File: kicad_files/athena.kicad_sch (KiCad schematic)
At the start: 540 parts, among them J1 SM04B-SRSS-TB(LF)(SN), J2 TYPE-C-31-M12, J3 SM04B-SRSS-TB(LF)(SN), Q1 DTC123JKAT146, Q2 AO3401A, SW1 K2-1187SQ-A4SW-06, SW10 MX Switch, SW100 MX Switch, SW101 MX Switch, SW102 MX Switch, SW103 MX Switch, SW104 MX Switch, SW105 MX Switch, SW106 MX Switch, SW107 MX Switch, SW108 MX Switch, SW109 MX Switch, SW11 MX Switch, SW110 MX Switch, SW111 MX Switch, SW112 MX Switch, SW113 MX Switch, SW12 MX Switch, SW13 MX Switch, SW14 MX Switch, SW15 MX Switch, SW16 MX Switch, SW17 MX Switch, SW18 MX Switch, SW19 MX Switch, SW2 MX Switch, SW20 MX Switch, SW21 MX Switch, SW22 MX Switch, SW23 MX Switch, SW24 MX Switch, SW25 MX Switch, SW26 MX Switch, SW27 MX Switch, SW28 MX Switch, SW29 MX Switch, SW3 MX Switch, SW30 MX Switch, SW31 MX Switch, SW32 MX Switch, SW33 MX Switch, SW34 MX Switch, SW35 MX Switch, SW36 MX Switch, SW37 MX Switch, SW38 MX Switch, SW39 MX Switch, SW4 MX Switch, SW40 MX Switch, SW41 MX Switch, SW42 MX Switch, SW43 MX Switch, SW44 MX Switch, SW45 MX Switch, SW46 MX Switch, SW47 MX Switch, SW48 MX Switch, SW49 MX Switch, SW5 MX Switch, SW50 MX Switch, SW51 MX Switch, SW52 MX Switch, SW53 MX Switch, SW54 MX Switch, SW55 MX Switch, SW56 MX Switch, SW57 MX Switch, SW58 MX Switch, SW59 MX Switch, SW6 MX Switch, SW60 MX Switch, SW61 MX Switch, SW62 MX Switch, SW63 MX Switch, SW64 MX Switch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

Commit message: Update component metadata
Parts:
- C16, C17, C5: Package C3216 -> C3216 (CASE A)
- D10, D11, D12, D13, D14, D15, D16, D17, D18, D19, D20, D21, D22, D23, D24, D25, D26, D27, D28, D29, D30, D31, D32, D33, D34, D35, D36, D4, D5, D6, D7, D8, D9: Manufacturer Part Number LCSC C965556 (https://www.lcsc.com/product-detail/Light-Emi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 -> WS2812C-2020; Vendor Part Number WS2812C-2020 -> LCSC C965556
- D2: LCSC Part Number C114257 -> (none); Vendor Part Number (none) -> LCSC C114257
- F1: LCSC Part Number C69691 -> (none); Vendor Part Number (none) -> LCSC C69691
- FB1, FB2: LCSC Part Number C139186 -> (none); Vendor Part Number (none) -> LCSC C139186
- J1, J3: LCSC Part Number C160404 -> (none); Vendor Part Number (none) -> LCSC C160404
- J2: LCSC Part Number C165948 -> (none); Specification (none) -> 16-pin USB 2.0 type C connector; Vendor Part Number (none) -> LCSC C165948
- Q1: LCSC Part Number C111724 -> (none); Vendor Part Number (none) -> LCSC C111724
- SW1: LCSC Part Number C92584 -> (none); Vendor Part Number (none) -> LCSC C92584
- SW10, SW100, SW101, SW102, SW103, SW104, SW105, SW106, SW107, SW108, SW109, SW11, SW110, SW111, SW112, SW113, SW12, SW13, SW14, SW15, SW16, SW17, SW18, SW19, SW2, SW20, SW21, SW22, SW23, SW24, SW25, SW26, SW27, SW28, SW29, SW3, SW30, SW31, SW32, SW33, SW34, SW35, SW36, SW37, SW38, SW39, SW4, SW40, SW41, SW42, SW43, SW44, SW45, SW46, SW47, SW48, SW49, SW5, SW50, SW51, SW52, SW53, SW54, SW55, SW56, SW57, SW58, SW59, SW6, SW60, SW61, SW62, SW63, SW64, SW65, SW66, SW67, SW68, SW69, SW7, SW70, SW71, SW72, SW73, SW74, SW75, SW76, SW77, SW78, SW79, SW8, SW80, SW81, SW82, SW83, SW84, SW85, SW86, SW87, SW88, SW89, SW9, SW90, SW91, SW92, SW93, SW94, SW95, SW96, SW97, SW98, SW99: Manufacturer Kaihua -> (none); Specification MX-style switch socket -> MX-style mechanical keyboard switch
- U3: LCSC Part Number C132604 -> (none); Vendor Part Number (none) -> LCSC C132604
- U4: LCSC Part Number C7519 -> (none); Vendor Part Number (none) -> LCSC C7519
- U5: LCSC Part Number C39051 -> (none); Vendor Part Number (none) -> LCSC C39051

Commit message: Re-routes, optimizations, corrections
- Re-routed rows R4 and R5; SWCLK pin confirmedly works as row pin as tested on pre-revision Alpha prototypes
- Removec trace stubs on bottom left
- Small traces optimization
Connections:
- net SWCLK is gone; now on net R5: U2.37 (PA14), X1.2 (Pin_2)
- net R4: now also U2.3 (PC14_OSC32IN)
- net R5: no longer U2.3 (PC14_OSC32IN)

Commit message: a-RC1 label, digital transistors
- Label was changed to Alpha-RC1 version
- Instead of relying on MCU open-drain pins, discrete digital NPN transistors were added to the caps lock indicator control and backlight PWM opendrain circuit
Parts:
- added Q3, Q4: DTC123JKAT146, Package_TO_SOT_SMD:SOT-23, symbol acheronSymbols:DTC123J
- GR6: renamed from GR4; footprint athena_library:athena_letters_pre-alpha_35x5.6 -> athena_library:athena_label_35x5.6
- renumbered C13 to C1, C6 to C10, C7 to C11, C16 to C12, C17 to C13, C19 to C14, C8 to C15, C9 to C16, C10 to C17, C11 to C18, C20 to C19, C14 to C2, C21 to C20, C22 to C21, C23 to C22, C24 to C23, C25 to C24, C26 to C25, C27 to C26, C28 to C27, C29 to C28, C30 to C29, C1 to C3, C31 to C30, C32 to C31, C33 to C32, C34 to C33, C35 to C34, C36 to C35, C37 to C36, C38 to C37, C39 to C38, C40 to C39, C2 to C4, C41 to C40, C42 to C41, C43 to C42, C44 to C43, C45 to C44, C46 to C45, C47 to C46, C48 to C47, C49 to C48, C50 to C49, C3 to C5, C51 to C50, C52 to C51, C15 to C6, C4 to C7, C18 to C8, C5 to C9, GR7 to GR2, GR2 to GR3, GR8 to GR4, GR3 to GR5, GR5 to GR7, GR6 to GR8, LED99 to LED100, LED100 to LED101, LED101 to LED102, LED102 to LED103, LED103 to LED104, LED104 to LED105, LED105 to LED106, LED106 to LED107, LED107 to LED108, LED108 to LED109, LED109 to LED110, LED69 to LED68, LED68 to LED69, LED94 to LED91, LED91 to LED92, LED92 to LED93, LED93 to LED94, LED110 to LED95, LED95 to LED96, LED96 to LED97, LED97 to LED98, LED98 to LED99, R11 to R10, R109 to R108, R110 to R109, R7 to R11, R108 to R110, R5 to R3, R3 to R4, R10 to R5, R4 to R6, R8 to R7, R9 to R8, R87 to R86, R88 to R87, R89 to R88, R90 to R89, R6 to R9, R91 to R90, R92 to R91, R93 to R92, R94 to R93, R95 to R94, R96 to R95, R97 to R96, R98 to R97, R86 to R98, U3 to U1, U4 to U2, U1 to U3, U2 to U4, X2 to X1, X1 to X2
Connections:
- net CAPS_INDICATOR: now also Q4.1 (B); no longer LED68.K, LED69.K
- net GND: now also Q3.2 (E), Q4.2 (E)
- net LED_PWM: now also Q3.1 (B); no longer R14.1, R15.1
- new net: Q3.3 (C), R14.1, R15.1
- new net: LED68.K, LED69.K, Q4.3 (C)

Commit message: Start porting to 64 pin MCU
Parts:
- removed C4, C5, C7: 100n, Capacitor_SMD:C_0402_1005Metric, symbol Device:C_Small
- removed R1, R2, R4: 1.5k, Resistor_SMD:R_0402_1005Metric, symbol Device:R_Small
- removed U4: STM32F411CEU6, acheron_Components:STM_UFQFPN-48_LQFP-48-1EP_7x7mm_P0.5mm_HandSoldering_ThermalReliefs, symbol acheron_Symbols:STM32F411-48
- added C15, C19: 4.7u, Capacitor_SMD:C_0402_1005Metric, symbol Device:C_Small
- added C16: 10n, Capacitor_SMD:C_0402_1005Metric, symbol Device:C_Small
- added C8: 100n, Capacitor_SMD:C_0402_1005Metric, symbol Device:C_Small
- added R7: 4.7k, Resistor_SMD:R_0402_1005Metric, symbol Device:R_Small
- added U5: STM32F401RCT6, acheron_Components:LQFP-64_10x10mm_P0.5mm, symbol acheronSymbols:STM32F401-LQFP64
- C10: value 1u -> 100n
- C11: value 10n -> 100n
- C18: value 4.7u -> 100n
- R6: value 0R -> 4.7k; footprint Resistor_SMD:R_0805_2012Metric -> Resistor_SMD:R_0402_1005Metric; Package R0805 -> R0402
- U3: value BL24C256A-SFRC -> 24LC256-I/SN; footprint acheron_Components:TSSOP-8_4.4x3mm_P0.65mm -> acheron_Components:SOIC-8; Manufacturer Shanghai Belling -> Microchip; Manufacturer Part Number BL24C256A-SFRC -> 24LC256-I/SN; Package TSSOP-8 -> SOIC-8; Specification TSSOP-8 non-volatile 256Kb (32K x 8) I2C EEPROM -> SOIC-8 non-volatile 256Kb (32K x 8) I2C EEPROM; Vendor Part Number LCSC C691875 (https://lcsc.com/product-detail/EEPROM_BL-Sha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 -> LCSC C411625
- renumbered C9 to C12, C15 to C13, C16 to C14, C19 to C20, C20 to C21, C21 to C22, C22 to C23, C23 to C24, C24 to C25, C25 to C26, C26 to C27, C27 to C28, C28 to C29, C29 to C30, C30 to C31, C31 to C32, C32 to C33, C33 to C34, C34 to C35, C35 to C36, C36 to C37, C37 to C38, C38 to C39, C6 to C4, C39 to C40, C40 to C41, C41 to C42, C42 to C43, C43 to C44, C44 to C45, C45 to C46, C46 to C47, C47 to C48, C48 to C49, C8 to C5, C49 to C50, C50 to C51, C51 to C52, C12 to C6, C13 to C7, C14 to C9, R3 to R1, R12 to R10, R102 to R100, R103 to R101, R104 to R102, R105 to R103, R106 to R104, R107 to R105, R108 to R106, R109 to R107, R110 to R108, R13 to R11, R14 to R12, R15 to R13, R16 to R14, R17 to R15, R18 to R16, R19 to R17, R20 to R18, R21 to R19, R5 to R2, R22 to R20, R23 to R21, R24 to R22, R25 to R23, R26 to R24, R27 to R25, R28 to R26, R29 to R27, R30 to R28, R31 to R29, R7 to R3, R32 to R30, R33 to R31, R34 to R32, R35 to R33, R36 to R34, R37 to R35, R38 to R36, R39 to R37, R40 to R38, R41 to R39, R8 to R4, R42 to R40, R43 to R41, R44 to R42, R45 to R43, R46 to R44, R47 to R45, R48 to R46, R49 to R47, R50 to R48, R51 to R49, R9 to R5, R52 to R50, R53 to R51, R54 to R52, R55 to R53, R56 to R54, R57 to R55, R58 to R56, R59 to R57, R60 to R58, R61 to R59, R62 to R60, R63 to R61, R64 to R62, R65 to R63, R66 to R64, R67 to R65, R68 to R66, R69 to R67, R70 to R68, R71 to R69, R72 to R70, R73 to R71, R74 to R72, R75 to R73, R76 to R74, R77 to R75, R78 to R76, R79 to R77, R80 to R78, R81 to R79, R10 to R8, R82 to R80, R83 to R81, R84 to R82, R85 to R83, R86 to R84, R87 to R85, R88 to R86, R89 to R87, R90 to R88, R91 to R89, R11 to R9, R92 to R90, R93 to R91, R94 to R92, R95 to R93, R96 to R94, R97 to R95, R98 to R96, R99 to R97, R100 to R98, R101 to R99, U5 to U4
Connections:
- net 3V3: now also C18.1, R6.2, C15.2, C16.2, C8.2, R7.2, U5.1 (VBAT), U5.13 (VDDA/VREF+), U5.19 (VDD), U5.32 (VDD), U5.48 (VDD), U5.64 (VDD)
- net 5V: no longer R6.1
- net BOOT0: now also C9.1, R10.1, R8.1, U5.60 (BOOT0); no longer C9.2, R10.2, R8.2
- net C0: now also U5.38 (USART6_RX/TIM3_CH2/PC7)
- net C1: now also U5.37 (I2S2_MCK/TIM3_CH1/USART6_TX/PC6)
- net C10: now also U5.20 (PA4/USART2_CK)
- net C11: now also U5.17 (PA3/TIM2_CH4/USART2_RX)
- net C12: now also U5.16 (PA2/TIM2_CH3/USART2_TX)
- net C13: now also U5.25 (PC5)
- net C14: now also U5.43 (USART1_RX/TIM1_CH3/PA10)
- net C15: now also U5.41 (USART1_CK/TIM1_CH1/PA8)
- net C16: now also U5.40 (TIM3_CH4/I2S_CKIN/PC9)
- net C2: now also U5.35 (SPI2_MISO/PB14)
- net C3: now also U5.33 (PB12)
- net C4: now also U5.29 (PB10/TIM2_CH3/SPI2_SCK/I2C2_SCL/I2S2_CK)
- net C5: now also U5.27 (PB1/TIM3_CH4)
- net C6: now also U5.24 (PC4)
- net C7: now also U5.23 (PA7/SPI1_MOSI/TIM3_CH2)
- net C8: now also U5.22 (PA6/TIM3_CH1/SPI1_MISO)
- net C9: now also U5.21 (PA5/TIM2_CH1/SPI1_SCK)
- net CAPS_INDICATOR: now also U5.39 (USART6_CK/TIM3_CH3/PC8)
- net D+: now also U5.45 (OTG_FS_DP/USART6_RX/PA12)
- net D-: now also U5.44 (OTG_FS_DM/TIM1_CH4/USART6_TX/PA11)
- net GND: now also C18.2, C9.2, R10.2, C15.1, C16.1, C19.1, C8.1, U5.12 (VSSA/VREF-), U5.18 (VSS), U5.31 (VSS), U5.47 (VSS), U5.63 (VSS); no longer C18.1, C9.1, R10.1
- net LED_PWM: now also U5.26 (PB0/TIM3_CH3)
- net NRST: now also U5.7 (NRST)
- net PA9: now also U5.42 (USART1_TX/TIM1_CH2/PA9); no longer R6.2
- net PB2/BOOT1: now also U5.28 (PB2)
- net R0: now also U5.52 (SPI3_MISO/PC11)
- net R1: now also U5.53 (SPI3_MOSI/PC12)
- net R2: now also U5.51 (SPI3_SCK/I2S3_CK/PC10)
- net R3: now also U5.50 (JTDI/TIM2_CH1/PA14)
- net R5: no longer X2.2 (Pin_2)
- net RGB_3V3: now also U5.36 (SPI2_MOSI/PB15)
- net SCL: now also R7.1, U5.58 (I2C1_SCL/USART1_TX/TIM4_CH1/PB6)
- net SDA: now also R6.1, U5.59 (I2C1_SDA/USART1_RX/TIM4_CH2/PB7)
- net SWDIO: now also U5.46 (JTMS-SWDIO/PA13)
- net XTAL_IN: now also U5.5 (PH0/OSC_IN)
- net XTAL_OUT: now also U5.6 (PH1/OSC_OUT)
- net at D3.1 (K): now also R8.2; no longer R8.1
- new net: C19.2, U5.30 (VCAP1)
- new net SWCLK: U5.49 (JTCK-SWCLK/PA14), X2.2 (Pin_2)
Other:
- note added: "SPOOKY PIN"
- note removed: "Spooky pin (*)"
- moved on the sheet: C12, C13, C14, C9, R10, R8, X2, Y1

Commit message: hange LDO caps to MLCC
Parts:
- removed C6, C7: 1u, acheron_Components:CP_EIA-3216-10_Kemet-I_Pad1.58x1.35mm_HandSolder, symbol Device:CP1
- added C6, C7: 1u, Capacitor_SMD:C_0805_2012Metric, symbol Device:C
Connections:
- net 3V3: now also C7.1
- net 5V: now also C6.1
- net GND: now also C6.2, C7.2
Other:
- moved on the sheet: C13, C14, Y1

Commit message: Update libs, route extra pins
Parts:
- added R12: 0R, Resistor_SMD:R_0805_2012Metric, symbol Device:R_Small
- renumbered R99 to R100, R100 to R101, R101 to R102, R102 to R103, R103 to R104, R104 to R105, R105 to R106, R106 to R107, R107 to R108, R108 to R109, R12 to R13, R13 to R14, R14 to R15, R15 to R16, R16 to R17, R17 to R18, R18 to R19, R19 to R20, R20 to R21, R21 to R22, R22 to R23, R23 to R24, R24 to R25, R25 to R26, R26 to R27, R27 to R28, R28 to R29, R29 to R30, R30 to R31, R31 to R32, R32 to R33, R33 to R34, R34 to R35, R35 to R36, R36 to R37, R37 to R38, R38 to R39, R39 to R40, R40 to R41, R41 to R42, R42 to R43, R43 to R44, R44 to R45, R45 to R46, R46 to R47, R47 to R48, R48 to R49, R49 to R50, R50 to R51, R51 to R52, R52 to R53, R53 to R54, R54 to R55, R55 to R56, R56 to R57, R57 to R58, R58 to R59, R59 to R60, R60 to R61, R61 to R62, R62 to R63, R63 to R64, R64 to R65, R65 to R66, R66 to R67, R67 to R68, R68 to R69, R69 to R70, R70 to R71, R71 to R72, R72 to R73, R73 to R74, R74 to R75, R75 to R76, R76 to R77, R77 to R78, R78 to R79, R79 to R80, R80 to R81, R81 to R82, R82 to R83, R83 to R84, R84 to R85, R85 to R86, R86 to R87, R87 to R88, R88 to R89, R89 to R90, R90 to R91, R91 to R92, R92 to R93, R93 to R94, R94 to R95, R95 to R96, R96 to R97, R97 to R98, R98 to R99
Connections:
- net 5V: now also R12.2
- net PA9: now also R12.1
- net R4: now also U5.14 (PA0/TIM2_CH1/USART2_CTS)
- net R5: now also U5.15 (PA1/TIM2_CH2/USART2_RTS)
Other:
- moved on the sheet: C1, C10, C11, C12, C13, C14, C15, C16, C17, C18, C19, C2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

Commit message: Add some extra pins
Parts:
- added J3: Conn_02x07_Counter_Clockwise, acheron_Connectors:PinHeader_2x3_P2.54mm_Vertical, symbol Connector_Generic:Conn_02x03_Odd_Even
- renumbered C8 to C1, C14 to C10, C9 to C11, C15 to C12, C16 to C13, C17 to C14, C18 to C15, C19 to C16, C1 to C17, C2 to C18, C4 to C19, C3 to C2, C10 to C3, C11 to C4, C12 to C6, C6 to C7, C7 to C8, C13 to C9, D2 to D1, D3 to D2, D1 to D3, J2 to J1, J3 to J2, J1 to J4, R6 to R1, R1 to R12, R7 to R2, R12 to R3, R2 to R4, R3 to R5, R4 to R6, R5 to R7, U2 to U1, U3 to U2, U5 to U3, U1 to U5
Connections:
- net 3V3: now also J3.4 (Pin_4)
- net C14: now also SW104.2; no longer SW104.1
- net GND: now also J3.2 (Pin_2)
- net R4: now also U3.8 (PC0); no longer U3.14 (PA0/TIM2_CH1/USART2_CTS)
- net at D126.2 (A): now also SW104.1; no longer SW104.2
- net E-PC2: now reaches U3.10 (PC2/SPI2_MISO)
- net E-PC2: now also J3.5 (Pin_5)
- net E-PC3: now reaches U3.11 (PC3/SPI2_MOSI)
- net E-PC3: now also J3.3 (Pin_3)
- net E-PC13: now reaches U3.2 (PC13)
- net E-PC14: now reaches U3.3 (PC14/OSC32_IN)
- net E-PC15: now reaches U3.4 (PC15/OSC32_OUT)
- net E-PD2: now reaches U3.54 (PD2)
- net E-PB3: now reaches U3.55 (JTDO-SWO/SPI1_SCK/SPI3_SCK/I2C2_SDA/TIM2_CH2/PB3)
- net E-PB4: now reaches U3.56 (NJTRST/SPI1_MISO/SPI3_MISO/I2C3_SDA/TIM3_CH1/PB4)
- net E-PB5: now reaches U3.57 (SPI1_MOSI/SPI3_MOSI/TIM3_CH2/PB5)
- net E-PB8: now reaches U3.61 (I2C1_SCL/TIM4_CH3/TIM10_CH1/PB8)
- net E-PB9: now reaches U3.62 (I2C1_SDA/TIM4_CH4/TIM11_CH1/PB9)
- net E-PC1: now reaches U3.9 (PC1)
- net E-PC1: now also J3.6 (Pin_6)
- new net E-PA0: J3.1 (Pin_1), U3.14 (PA0/TIM2_CH1/USART2_CTS)
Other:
- moved on the sheet: SW104

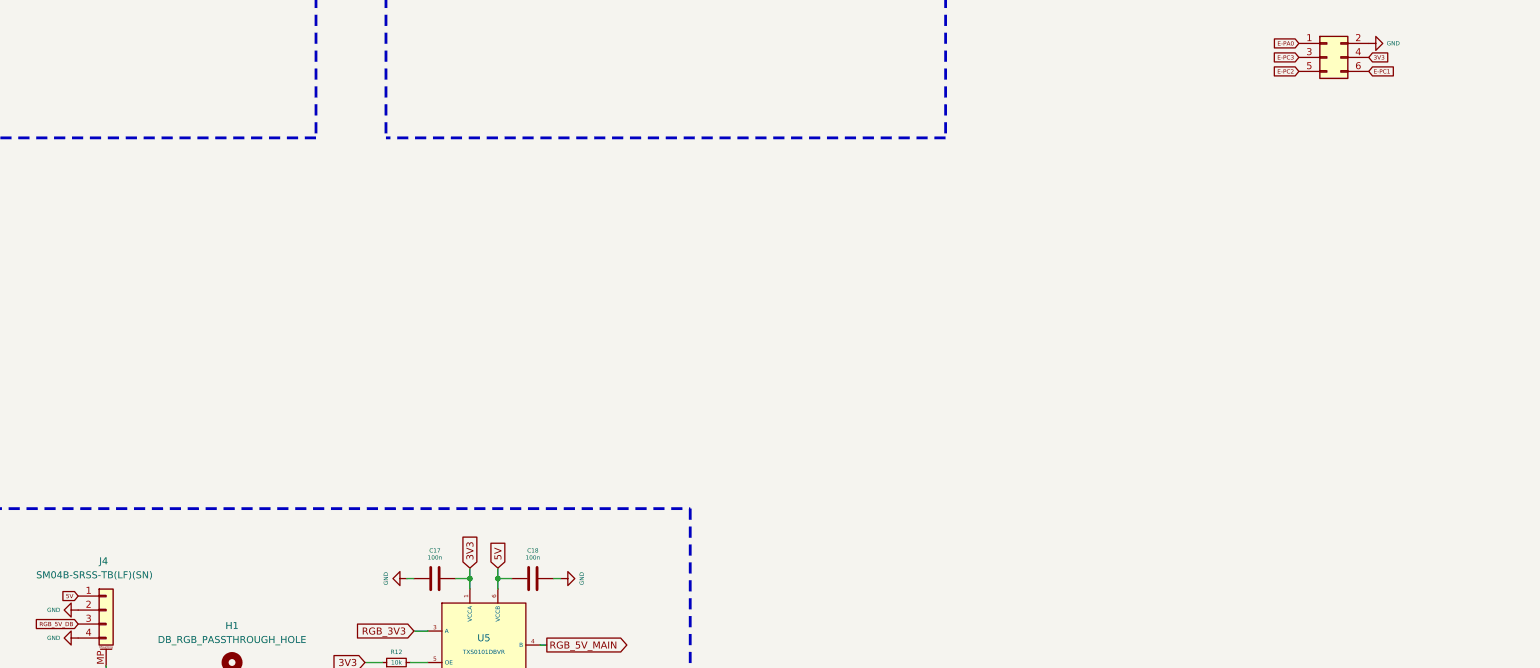
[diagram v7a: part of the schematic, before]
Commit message: Finish adding extra pins
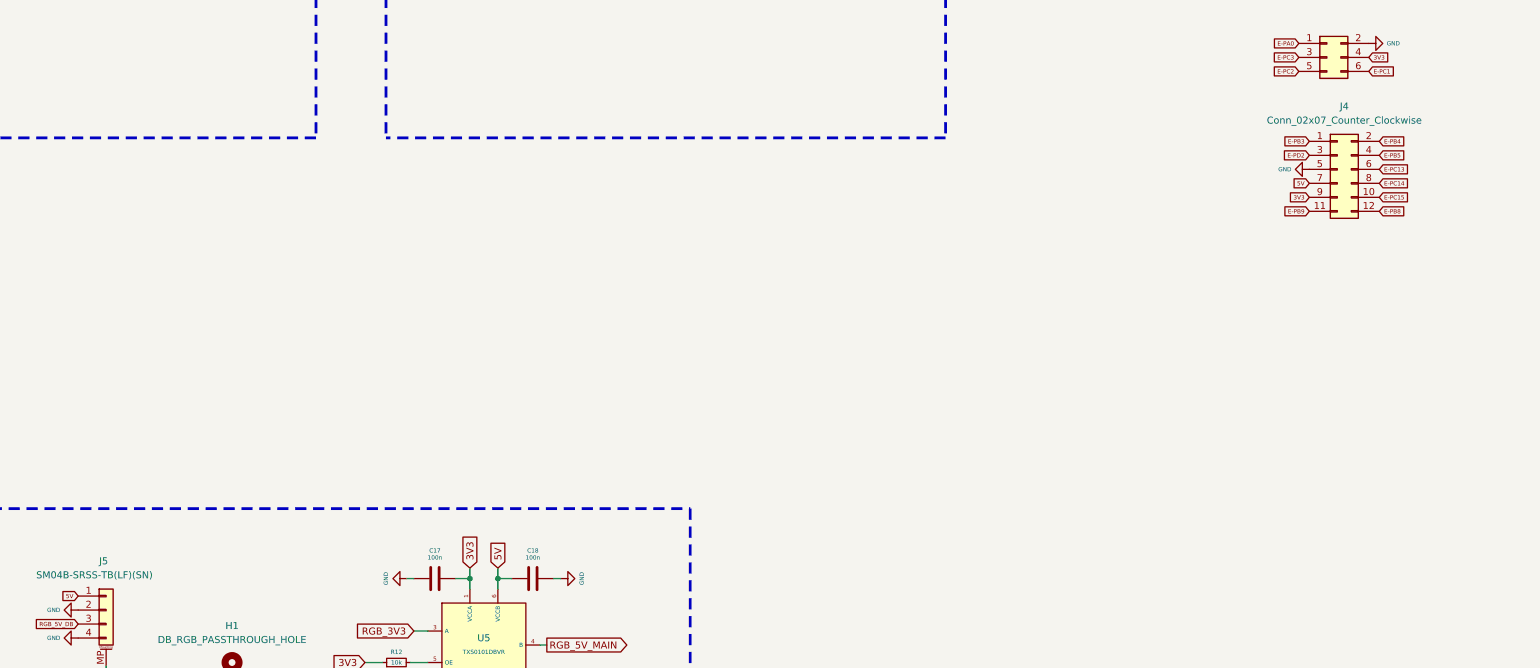
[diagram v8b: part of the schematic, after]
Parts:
- added J4: Conn_02x07_Counter_Clockwise, acheron_Connectors:PinHeader_2x6_P2.54mm_Vertical, symbol Connector_Generic:Conn_02x06_Odd_Even
- renumbered J4 to J5
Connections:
- net 3V3: now also J4.9 (Pin_9)
- net 5V: now also J4.7 (Pin_7)
- net E-PB3: now also J4.1 (Pin_1)
- net E-PB4: now also J4.2 (Pin_2)
- net E-PB5: now also J4.4 (Pin_4)
- net E-PB8: now also J4.12 (Pin_12)
- net E-PB9: now also J4.11 (Pin_11)
- net E-PC13: now also J4.6 (Pin_6)
- net E-PC14: now also J4.8 (Pin_8)
- net E-PC15: now also J4.10 (Pin_10)
- net E-PD2: now also J4.3 (Pin_3)
- net GND: now also J4.5 (Pin_5)
